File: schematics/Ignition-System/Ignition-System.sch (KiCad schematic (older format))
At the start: 10 parts

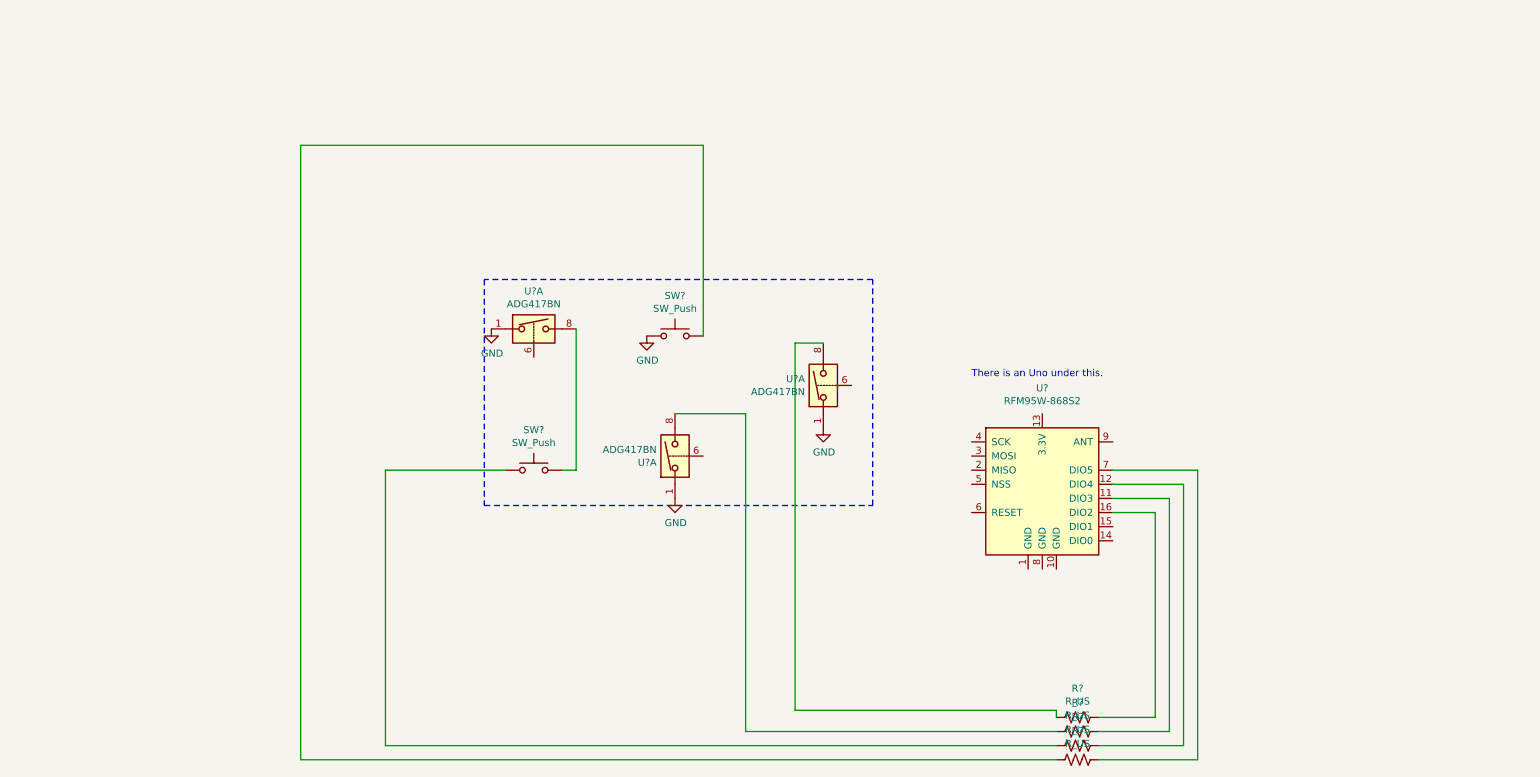
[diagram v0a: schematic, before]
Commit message: schema: Update Ignition-System
Updated schematic to match current control surfaces and plans for
extensions to the ground interface.
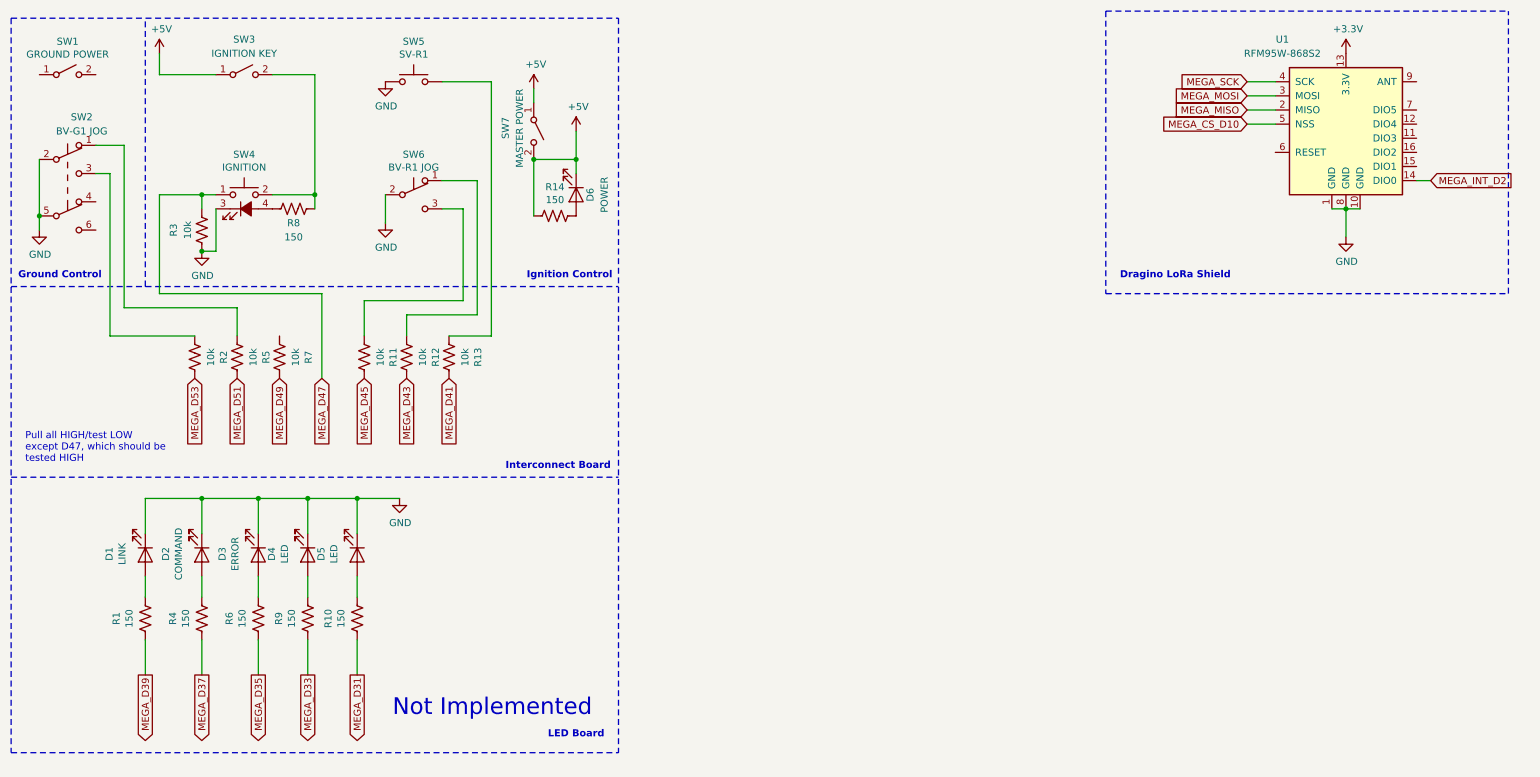
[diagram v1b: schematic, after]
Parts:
- removed SW?: SW_Push, symbol Switch:SW_Push
- removed U? (x3): ADG417BN, Package_DIP:DIP-8_W7.62mm, symbol Analog_Switch:ADG417BN
- added D1: LINK, symbol Device:LED
- added D2: COMMAND, symbol Device:LED
- added D3: ERROR, symbol Device:LED
- added D4, D5: LED, symbol Device:LED
- added D6: POWER, symbol Device:LED
- added R1, R10, R14, R4, R6, R8, R9: 150, symbol Device:R_US
- added R2, R5, R7: 10k, symbol Device:R_US
- added SW1: GROUND POWER, symbol Switch:SW_SPST
- added SW2: BV-G1 JOG, symbol Switch:SW_Push_DPDT
- added SW3: IGNITION KEY, symbol Switch:SW_SPST
- added SW4: IGNITION, symbol Switch:SW_Push_LED
- added SW6: BV-R1 JOG, symbol Switch:SW_Push_SPDT
- added SW7: MASTER POWER, symbol Switch:SW_SPST
- R11, R12, R13, R3: renamed from R?; value R_US -> 10k
- SW5: renamed from SW?; value SW_Push -> SV-R1
- gave numbers to parts that had none: 1
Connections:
- net GND: now also R3.1, U1.1 (GND), U1.10 (GND), U1.8 (GND), D1.1 (K), D2.1 (K), D3.1 (K), D4.1 (K), D5.1 (K), SW2.2 (B), SW2.5 (B), SW4.3 (K), SW6.2 (B)
- net MEGA_D47: now reaches R3.2
- net MEGA_D47: now also SW4.1
- net at R12.2: now also SW6.1 (A)
- net at R11.2: now also SW6.3 (C)
- net at U1.11 (DIO3): no longer R11.1
- net at U1.12 (DIO4): no longer R12.1
- net +3V3: now reaches U1.13 (3.3V)
- net MEGA_INT_D2: now reaches U1.14 (DIO0)
- net at U1.16 (DIO2): no longer R3.1
- net MEGA_MISO: now reaches U1.2 (MISO)
- net MEGA_MOSI: now reaches U1.3 (MOSI)
- net MEGA_SCK: now reaches U1.4 (SCK)
- net MEGA_CS_D10: now reaches U1.5 (NSS)
- net at U1.7 (DIO5): no longer R13.1
- new net: R8.1, SW3.2 (B), SW4.2
- new net: R8.2, SW4.4 (A)
- new net: R5.2, SW2.1 (A)
- new net: R2.2, SW2.3 (C)
- new net: D1.2 (A), R1.1
- new net: D2.2 (A), R4.1
- new net: D3.2 (A), R6.1
- new net: D4.2 (A), R9.1
- new net: D5.2 (A), R10.1
- new net: D6.2 (A), R14.1
- new net +5V: D6.1 (K), R14.2, SW3.1 (A), SW7.1 (A), SW7.2 (B)
- new net MEGA_D31: R10.2
- new net MEGA_D33: R9.2
- new net MEGA_D35: R6.2
- new net MEGA_D37: R4.2
- new net MEGA_D39: R1.2
- new net MEGA_D41: R13.1
- new net MEGA_D43: R12.1
- new net MEGA_D45: R11.1
- new net MEGA_D49: R7.1
- new net MEGA_D51: R5.1
- new net MEGA_D53: R2.1
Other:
- note added: "Dragino LoRa Shield"
- note added: "Ground Control"
- note added: "Ignition Control\n"
- note added: "Interconnect Board"
- note added: "LED Board"
- note added: "Not Implemented\n"
- note added: "Pull all HIGH/test LOW \nexcept D47, which should be\ntested HIGH"
- note removed: "There is an Uno under this."
- moved on the sheet: R11, R12, R13, R3, SW5, U1

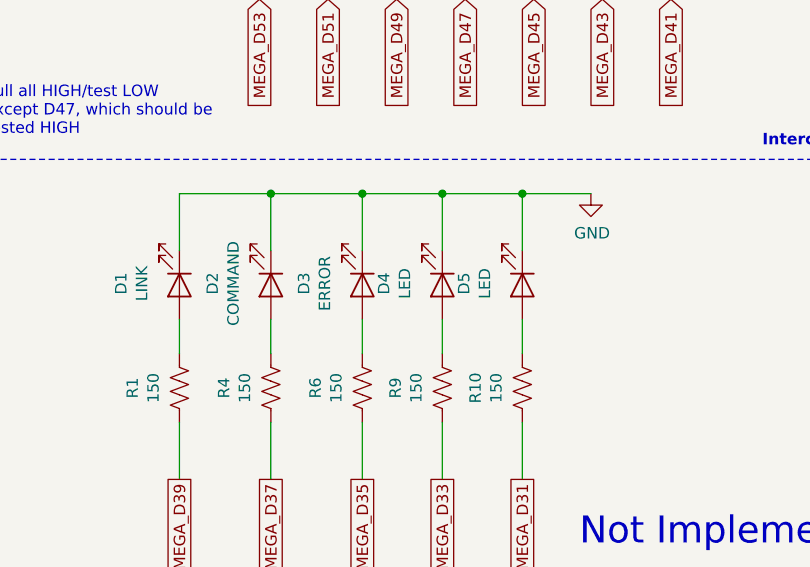
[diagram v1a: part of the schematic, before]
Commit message: specs/Prop-Avionics: Update with I2C protocol defs
Added basic I2c protocol specs to standardize implementation across all
devices that will communicate on this bus. Design is still pending and
may not work as speced.
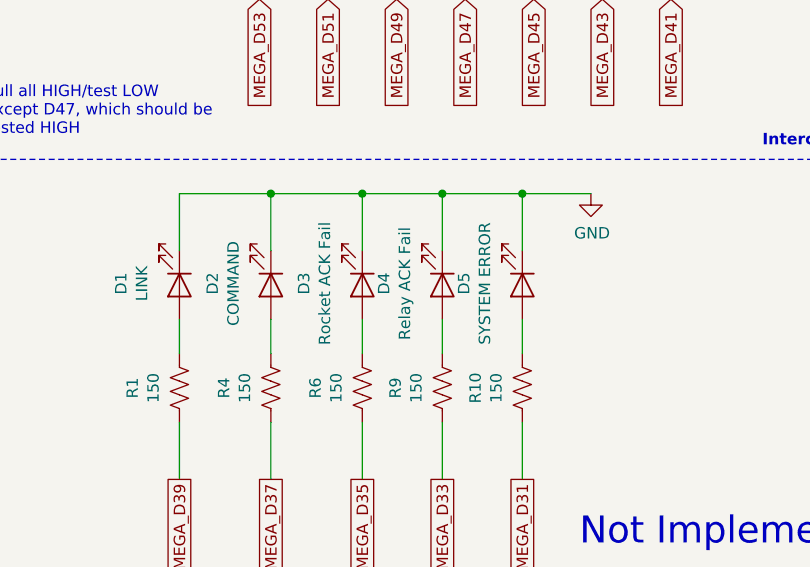
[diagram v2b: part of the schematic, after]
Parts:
- D3: value ERROR -> Rocket ACK Fail
- D4: value LED -> Relay ACK Fail
- D5: value LED -> SYSTEM ERROR
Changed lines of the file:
@@
 P 3000 4350
 F 0 "D5" H 2993 4095 50  0000 C CNN
-F 1 "LED" H 2993 4186 50  0000 C CNN
+F 1 "SYSTEM ERROR" H 2993 4186 50  0000 C CNN
 F 2 "" H 3000 4350 50  0001 C CNN
 F 3 "~" H 3000 4350 50  0001 C CNN
@@
 P 2650 4350
 F 0 "D4" H 2643 4095 50  0000 C CNN
-F 1 "LED" H 2643 4186 50  0000 C CNN
+F 1 "Relay ACK Fail" H 2643 4186 50  0000 C CNN
 F 2 "" H 2650 4350 50  0001 C CNN
 F 3 "~" H 2650 4350 50  0001 C CNN
@@
 P 2300 4350
 F 0 "D3" H 2293 4095 50  0000 C CNN
-F 1 "ERROR" H 2293 4186 50  0000 C CNN
+F 1 "Rocket ACK Fail" H 2293 4186 50  0000 C CNN
 F 2 "" H 2300 4350 50  0001 C CNN
 F 3 "~" H 2300 4350 50  0001 C CNN
